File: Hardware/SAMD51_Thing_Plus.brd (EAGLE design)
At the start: 22.9 x 58.4 mm, 114 parts, among them J6 AMP FCI 10103594-0001LF, Q1 2.5A/30V, U1 MCP73831, U2 ATSAMD51J20A-A, U3 AP2112K-3.3V, U4 4MB Flash, Y1 32.768kHz

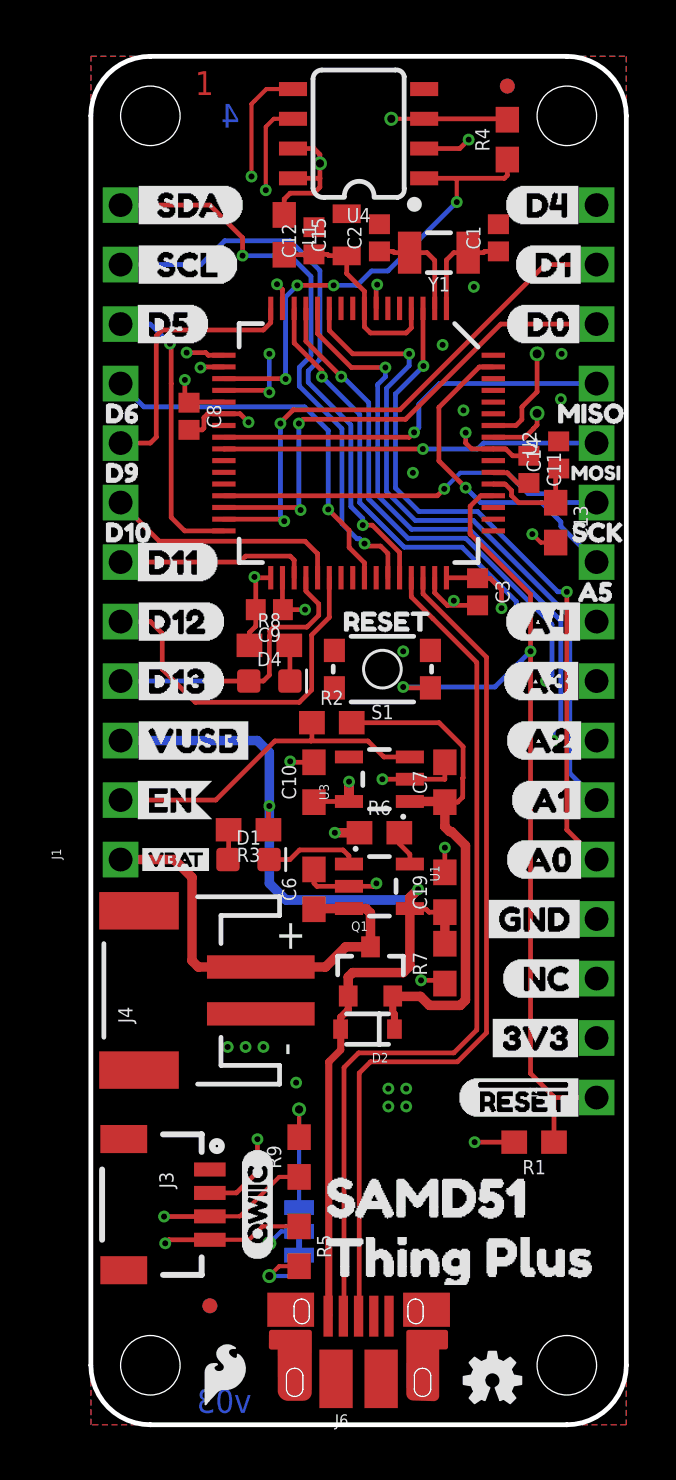
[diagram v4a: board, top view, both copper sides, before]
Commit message: adding i2c labels from double check
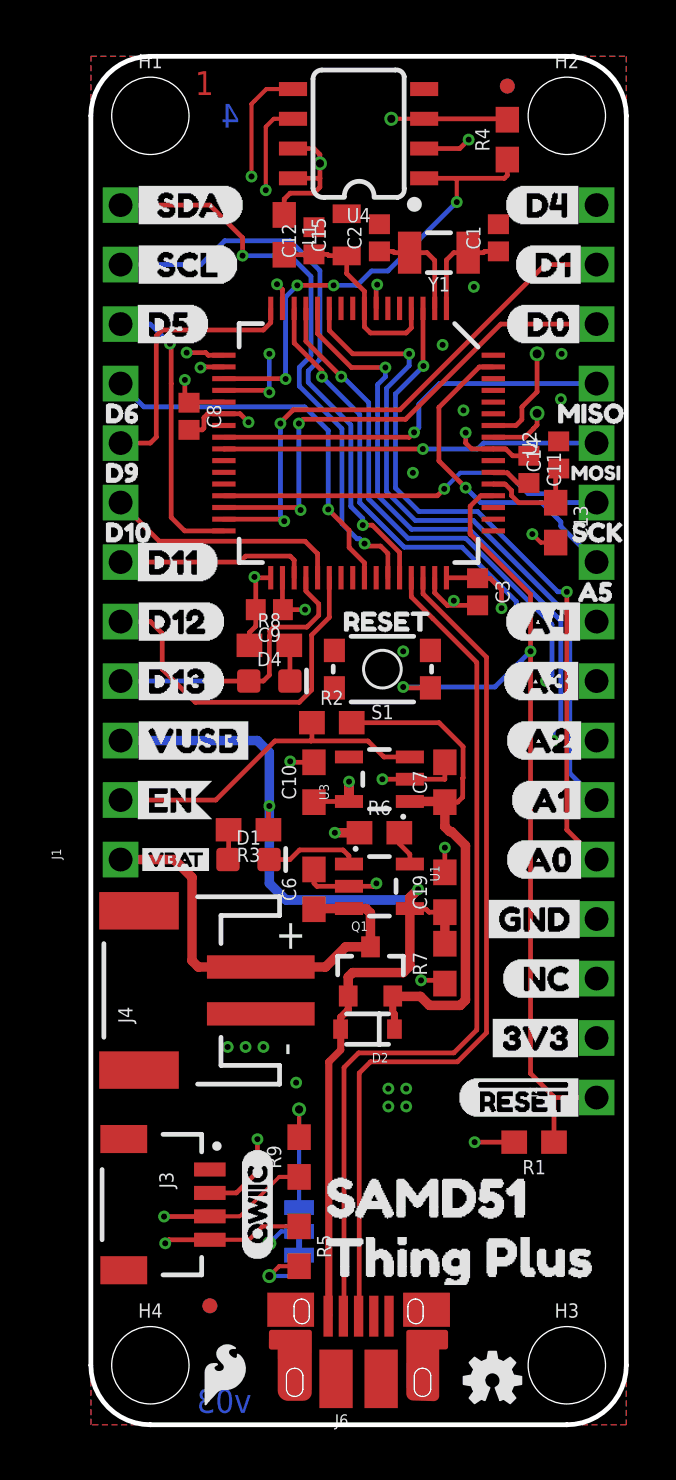
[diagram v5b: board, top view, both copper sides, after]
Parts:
- added H1, H2, H3, H4: STAND-OFF, SparkFun-Hardware:STAND-OFF
- added U$67: (no value), buzzard_labels (39):I_C0
- added U$68: (no value), buzzard_labels (39):21
- turned D1 to 0 degrees
- turned D4 to 0 degrees
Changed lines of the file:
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@@
 <wire x1="0" y1="2.54" x2="0" y2="55.88" width="0.2032" layer="20"/>
 <wire x1="0" y1="55.88" x2="2.54" y2="58.42" width="0.2032" layer="20" curve="-90"/>
-<hole x="2.54" y="55.88" drill="2.54"/>
-<hole x="20.32" y="55.88" drill="2.54"/>
-<hole x="20.32" y="2.54" drill="2.54"/>
-<hole x="2.54" y="2.54" drill="2.54"/>
 <text x="4.445" y="56.769" size="1.016" layer="1" font="vector" ratio="20">1</text>
 <text x="5.461" y="56.769" size="1.016" layer="2" font="vector" ratio="20">2</text>
@@
 <attribute name="PROD_ID" value="SWCH-13065" x="12.446" y="32.258" size="1.778" layer="27" font="vector" ratio="15" rot="R180" display="off"/>
 </element>
-<element name="FRAME1" library="SparkFun-Aesthetics" package="CREATIVE_COMMONS" value="FRAME-LEDGER" x="-17.145" y="-19.05"/>
+<element name="FRAME1" library="SparkFun-Aesthetics" package="CREATIVE_COMMONS" value="FRAME-LEDGER" x="-17.145" y="-19.05">
+<attribute name="DESIGNER" value="" x="-17.145" y="-19.05" size="1.778" layer="27" display="off"/>
+<attribute name="REV" value="" x="-17.145" y="-19.05" size="1.778" layer="27" display="off"/>
+</element>
 <element name="C7" library="SparkFun-Capacitors" package="0603" value="1.0uF" x="15.113" y="27.432" rot="R90">
 <attribute name="PROD_ID" value="CAP-13930" x="32.893" y="13.462" size="1.778" layer="27" font="vector" ratio="15" rot="R90" display="off"/>
@@
 <attribute name="PROD_ID" value="RES-00824" x="37.973" y="-13.335" size="1.778" layer="27" font="vector" ratio="15" rot="R90" display="off"/>
 </element>
-<element name="D1" library="SparkFun-LED" package="LED-0603" value="Yellow" x="6.731" y="24.13" rot="R270">
-<attribute name="PROD_ID" value="DIO-09003" x="-23.749" y="59.69" size="1.778" layer="27" font="vector" ratio="15" rot="R270" display="off"/>
+<element name="D1" library="SparkFun-LED" package="LED-0603" value="Yellow" x="6.731" y="24.13">
+<attribute name="PROD_ID" value="DIO-09003" x="-28.829" y="-6.35" size="1.778" layer="27" font="vector" ratio="15" display="off"/>
 </element>
 <element name="R3" library="SparkFun-Resistors" package="0603" value="1K" x="6.731" y="25.4" rot="R180">
@@
 <attribute name="PROD_ID" value="CAP-08280" x="51.943" y="-26.797" size="1.778" layer="27" font="vector" ratio="15" rot="R90" display="off"/>
 </element>
-<element name="D4" library="SparkFun-LED" package="LED-0603" value="BLUE" x="7.62" y="31.75" rot="R270">
-<attribute name="PROD_ID" value="DIO-08575" x="7.62" y="31.75" size="1.778" layer="27" font="vector" ratio="15" rot="R270" display="off"/>
+<element name="D4" library="SparkFun-LED" package="LED-0603" value="BLUE" x="7.62" y="31.75">
+<attribute name="PROD_ID" value="DIO-08575" x="7.62" y="31.75" size="1.778" layer="27" font="vector" ratio="15" display="off"/>
 </element>
 <element name="R8" library="SparkFun-Resistors" package="0603" value="330" x="7.62" y="33.274">
@@
 </element>
 <element name="JP1" library="SparkFun-Jumpers" package="SMT-JUMPER_3_2-NC_TRACE_SILK" value="JUMPER-SMT_3_2-NC_TRACE_SILK" x="8.89" y="8.255" rot="MR270"/>
+<element name="H1" library="SparkFun-Hardware" package="STAND-OFF" value="STAND-OFF" x="2.54" y="55.88"/>
+<element name="H2" library="SparkFun-Hardware" package="STAND-OFF" value="STAND-OFF" x="20.32" y="55.88"/>
+<element name="H3" library="SparkFun-Hardware" package="STAND-OFF" value="STAND-OFF" x="20.32" y="2.54"/>
+<element name="H4" library="SparkFun-Hardware" package="STAND-OFF" value="STAND-OFF" x="2.54" y="2.54"/>
+<element name="U$67" library="buzzard_labels (39)" package="I_C0" value="" x="6.858" y="9.906" rot="MR270"/>
+<element name="U$68" library="buzzard_labels (39)" package="21" value="" x="6.096" y="9.017" rot="MR270"/>
 </elements>
 <signals>
@@
 <wire x1="5.08" y1="52.07" x2="1.27" y2="52.07" width="0.2032" layer="1"/>
 <contactref element="R9" pad="1"/>
-<wire x1="5.08" y1="8.898" x2="6.358" y2="8.898" width="0.1778" layer="1"/>
-<wire x1="8.04" y1="10.58" x2="8.89" y2="10.58" width="0.1778" layer="1"/>
-<wire x1="6.358" y1="8.898" x2="8.04" y2="10.58" width="0.1778" layer="1"/>
+<wire x1="6.342" y1="8.898" x2="5.08" y2="8.898" width="0.1778" layer="1"/>
+<wire x1="8.89" y1="10.58" x2="8.04" y2="10.58" width="0.1778" layer="1"/>
+<wire x1="8.04" y1="10.58" x2="6.358" y2="8.898" width="0.1524" layer="1"/>
+<wire x1="6.358" y1="8.898" x2="6.342" y2="8.898" width="0.1524" layer="1"/>
 </signal>
 <signal name="A0">
@@
 <mfgpreviewcolor name="substratecolor" color="0xFF786E46"/>
 </mfgpreviewcolors>
-<errors>
-</errors>
 </board>
 </drawing>

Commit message: pre-design review changes
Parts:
- J3: device SparkFun-Connectors:1X04_1MM_RA -> SparkFun-Connectors:JST04_1MM_RA
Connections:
- net D1: now also U2.29; no longer U2.31
- net FLASH_MOSI: now also U2.17; no longer U2.18
- net FLASH_SCK: now also U2.18; no longer U2.17
- net SCK: now also U2.26; no longer U2.29
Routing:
- net D1: track 23.2 -> 21.6 mm
- net FLASH_MOSI: track 15.2 -> 14.5 mm
- net FLASH_SCK: track 14.9 -> 15.4 mm
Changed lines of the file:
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@@
 <element name="FD1" library="SparkFun-Aesthetics" package="MICRO-FIDUCIAL" value="FIDUCIALUFIDUCIAL" x="5.08" y="5.08"/>
 <element name="FD2" library="SparkFun-Aesthetics" package="MICRO-FIDUCIAL" value="FIDUCIALUFIDUCIAL" x="17.78" y="57.15"/>
-<element name="J3" library="SparkFun-Connectors" package="1X04_1MM_RA" value="" x="5.08" y="9.398" rot="R270">
+<element name="J3" library="SparkFun-Connectors" package="JST04_1MM_RA" value="" x="5.08" y="9.398" rot="R270">
 <attribute name="PROD_ID" value="CONN-13694" x="5.08" y="9.398" size="1.778" layer="27" font="vector" ratio="15" rot="R270" display="off"/>
 </element>
@@
 <via x="18.8468" y="38.0238" extent="1-16" drill="0.254"/>
 <via x="16.35125" y="48.5775" extent="1-16" drill="0.254"/>
-<via x="13.74775" y="40.64" extent="1-16" drill="0.254"/>
+<via x="13.74775" y="40.259" extent="1-16" drill="0.254"/>
 <wire x1="19.84375" y1="37.66275" x2="19.20785" y2="37.66275" width="0.1778" layer="1"/>
 <wire x1="19.20785" y1="37.66275" x2="18.8468" y2="38.0238" width="0.1778" layer="1"/>
@@
 <signal name="FLASH_SCK">
 <contactref element="U4" pad="6"/>
-<contactref element="U2" pad="17"/>
 <wire x1="7.487" y1="52.705" x2="7.4676" y2="52.705" width="0.2032" layer="1"/>
 <via x="7.4676" y="52.705" extent="1-16" drill="0.254"/>
-<via x="4.0894" y="45.7708" extent="1-16" drill="0.254"/>
+<via x="4.0894" y="45.2628" extent="1-16" drill="0.254"/>
 <wire x1="5.969" y1="52.705" x2="4.1148" y2="50.8508" width="0.2032" layer="2"/>
 <wire x1="5.969" y1="52.705" x2="7.4676" y2="52.705" width="0.2032" layer="2"/>
-<wire x1="4.0894" y1="45.7708" x2="4.1148" y2="45.7454" width="0.2032" layer="2"/>
-<wire x1="4.1148" y1="50.8508" x2="4.1148" y2="45.7454" width="0.2032" layer="2"/>
+<wire x1="4.0894" y1="45.2628" x2="4.1148" y2="45.2374" width="0.2032" layer="2"/>
+<wire x1="4.1148" y1="50.8508" x2="4.1148" y2="45.2374" width="0.2032" layer="2"/>
 <wire x1="7.4676" y1="52.705" x2="7.4676" y2="55.4101" width="0.1778" layer="1"/>
 <wire x1="7.8105" y1="55.753" x2="8.63" y2="55.753" width="0.1778" layer="1"/>
 <wire x1="7.4676" y1="55.4101" x2="7.8105" y2="55.753" width="0.1778" layer="1"/>
-<wire x1="5.68" y1="45.66" x2="5.013" y2="45.66" width="0.2032" layer="1"/>
-<wire x1="4.9022" y1="45.7708" x2="4.0894" y2="45.7708" width="0.2032" layer="1"/>
-<wire x1="5.013" y1="45.66" x2="4.9022" y2="45.7708" width="0.2032" layer="1"/>
+<contactref element="U2" pad="18"/>
+<wire x1="5.68" y1="45.16" x2="4.1922" y2="45.16" width="0.2032" layer="1"/>
+<wire x1="4.1922" y1="45.16" x2="4.0894" y2="45.2628" width="0.2032" layer="1"/>
 </signal>
 <signal name="V_USB">
@@
 <signal name="FLASH_MOSI">
 <contactref element="U4" pad="5"/>
-<contactref element="U2" pad="18"/>
 <via x="6.858" y="53.2892" extent="1-16" drill="0.254"/>
-<wire x1="4.8875" y1="45.16" x2="5.68" y2="45.16" width="0.2032" layer="1"/>
-<via x="4.67955" y="45.12985" extent="1-16" drill="0.254"/>
+<via x="4.67955" y="45.89185" extent="1-16" drill="0.254"/>
 <wire x1="6.858" y1="53.2892" x2="4.699" y2="51.1302" width="0.2032" layer="15"/>
-<wire x1="4.699" y1="45.1493" x2="4.67955" y2="45.12985" width="0.2032" layer="15"/>
-<wire x1="4.699" y1="51.1302" x2="4.699" y2="45.1493" width="0.2032" layer="15"/>
-<wire x1="4.67955" y1="45.12985" x2="4.85735" y2="45.12985" width="0.2032" layer="1"/>
-<wire x1="4.85735" y1="45.12985" x2="4.8875" y2="45.16" width="0.2032" layer="1"/>
+<wire x1="4.699" y1="45.9113" x2="4.67955" y2="45.89185" width="0.2032" layer="15"/>
+<wire x1="4.699" y1="51.1302" x2="4.699" y2="45.9113" width="0.2032" layer="15"/>
 <wire x1="8.63" y1="57.023" x2="7.493" y2="57.023" width="0.1778" layer="1"/>
-<wire x1="7.493" y1="57.023" x2="6.985" y2="56.515" width="0.1778" layer="1"/>
-<wire x1="6.858" y1="56.388" x2="6.985" y2="56.515" width="0.1778" layer="1"/>
+<wire x1="7.493" y1="57.023" x2="6.858" y2="56.388" width="0.1778" layer="1"/>
 <wire x1="6.858" y1="53.2892" x2="6.858" y2="56.388" width="0.1778" layer="1"/>
+<contactref element="U2" pad="17"/>
+<wire x1="4.67955" y1="45.89185" x2="4.9114" y2="45.66" width="0.2032" layer="1"/>
+<wire x1="4.9114" y1="45.66" x2="5.68" y2="45.66" width="0.2032" layer="1"/>
 </signal>
 <signal name="N$17">
@@
 <signal name="SCK">
 <contactref element="J2" pad="11"/>
-<contactref element="U2" pad="29"/>
 <wire x1="21.59" y1="39.37" x2="20.22381875" y2="39.37" width="0.2032" layer="16"/>
 <wire x1="20.22381875" y1="39.37" x2="19.84281875" y2="39.751" width="0.2032" layer="16"/>
 <wire x1="18.669" y1="39.751" x2="17.78" y2="40.64" width="0.2032" layer="16"/>
 <wire x1="19.84281875" y1="39.751" x2="18.669" y2="39.751" width="0.2032" layer="16"/>
-<via x="15.0876" y="39.9542" extent="1-16" drill="0.254"/>
-<wire x1="15.0876" y1="39.9542" x2="14.7934" y2="39.66" width="0.2032" layer="1"/>
-<wire x1="14.7934" y1="39.66" x2="5.68" y2="39.66" width="0.2032" layer="1"/>
-<wire x1="17.78" y1="40.64" x2="15.7734" y2="40.64" width="0.1778" layer="16"/>
-<wire x1="15.7734" y1="40.64" x2="15.0876" y2="39.9542" width="0.1778" layer="16"/>
+<via x="14.3256" y="40.8432" extent="1-16" drill="0.254"/>
+<wire x1="17.78" y1="40.64" x2="14.5288" y2="40.64" width="0.1778" layer="16"/>
+<wire x1="14.5288" y1="40.64" x2="14.3256" y2="40.8432" width="0.1778" layer="16"/>
+<contactref element="U2" pad="26"/>
+<wire x1="14.3256" y1="40.8432" x2="14.0088" y2="41.16" width="0.2032" layer="1"/>
+<wire x1="14.0088" y1="41.16" x2="5.68" y2="41.16" width="0.2032" layer="1"/>
 </signal>
 <signal name="MOSI">
@@
 <signal name="D1">
 <contactref element="J2" pad="15"/>
-<contactref element="U2" pad="31"/>
 <wire x1="19.3929" y1="49.53" x2="13.1913" y2="43.3284" width="0.2032" layer="1"/>
 <via x="8.0930125" y="42.7442" extent="1-16" drill="0.254"/>
 <wire x1="8.638425" y1="43.3284" x2="8.0930125" y2="42.7829875" width="0.2032" layer="1"/>
 <wire x1="13.1913" y1="43.3284" x2="8.638425" y2="43.3284" width="0.2032" layer="1"/>
-<wire x1="8.0930125" y1="42.7442" x2="8.0930125" y2="38.7377875" width="0.2032" layer="16"/>
-<via x="8.255" y="38.5758" extent="1-16" drill="0.254"/>
-<wire x1="5.68" y1="38.66" x2="8.1708" y2="38.66" width="0.2032" layer="1"/>
-<wire x1="8.1708" y1="38.66" x2="8.255" y2="38.5758" width="0.2032" layer="1"/>
-<wire x1="8.0930125" y1="38.7377875" x2="8.255" y2="38.5758" width="0.2032" layer="16"/>
+<wire x1="8.0930125" y1="42.7442" x2="8.0930125" y2="40.0077875" width="0.2032" layer="16"/>
 <wire x1="8.0930125" y1="42.7829875" x2="8.0930125" y2="42.7442" width="0.2032" layer="1"/>
 <wire x1="21.59" y1="49.53" x2="19.3929" y2="49.53" width="0.2032" layer="1"/>
+<contactref element="U2" pad="29"/>
+<wire x1="8.0930125" y1="40.0077875" x2="7.836225" y2="39.751" width="0.2032" layer="16"/>
+<wire x1="7.836225" y1="39.751" x2="7.62" y2="39.751" width="0.2032" layer="16"/>
+<via x="7.62" y="39.751" extent="1-16" drill="0.254"/>
+<wire x1="7.62" y1="39.751" x2="7.529" y2="39.66" width="0.2032" layer="1"/>
+<wire x1="7.529" y1="39.66" x2="5.68" y2="39.66" width="0.2032" layer="1"/>
 </signal>
 <signal name="D7">

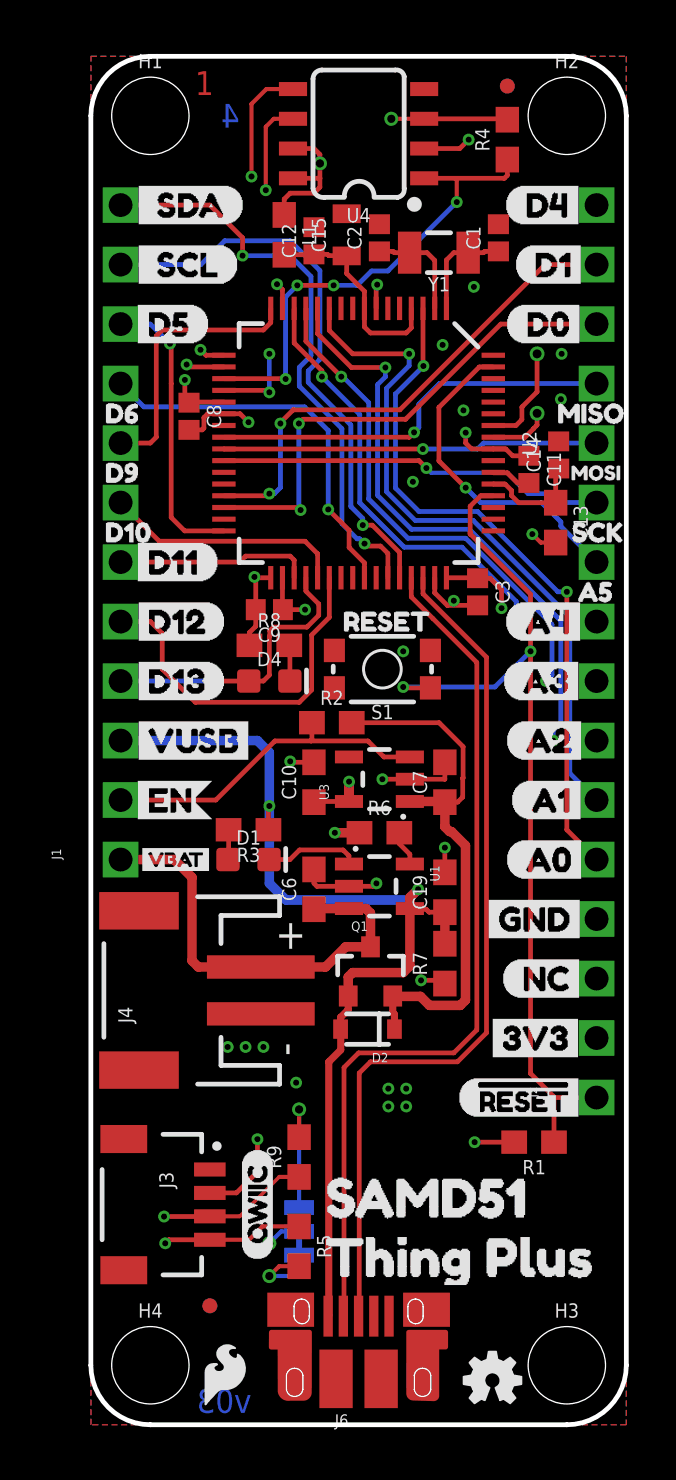
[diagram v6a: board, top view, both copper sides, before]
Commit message: engineer run of checklist-REDS
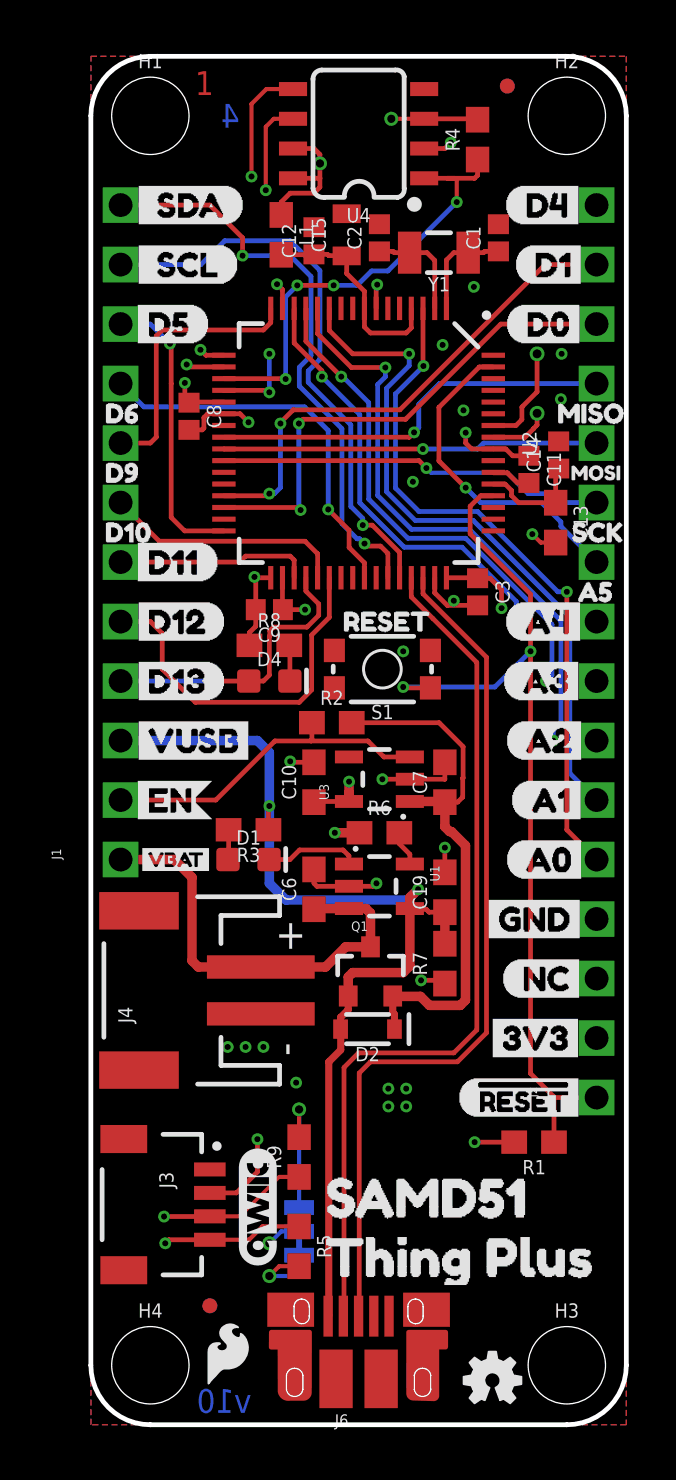
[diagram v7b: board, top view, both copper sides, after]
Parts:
- removed U$45: (no value), buzzard_labels (46):D14
- added U$69: QWIIC_LOGO_5MM, SparkFun-Aesthetics:QWIIC_5MM
- D2: value BAT20J -> 1A/23V/620mV
- FD1, FD2, FD3, FD4: device SparkFun-Aesthetics:MICRO-FIDUCIAL -> SparkFun-Aesthetics:FIDUCIAL-MICRO
- Q1: device SparkFun-DiscreteSemi:SOT23-3 -> SparkFun-DiscreteSemi:SOT23-3@1
- U$41: device buzzard_labels (46):SCK8 -> buzzard_labels (10):21#SCL1
- U$42: device buzzard_labels (46):MOSI7 -> buzzard_labels (10):22#MISO4
- U$43: device buzzard_labels (46):MISO6 -> buzzard_labels (10):23#MOSI3
- U$44: device buzzard_labels (46):D05 -> buzzard_labels (11):1#TX1
- U$47: device buzzard_labels (46):SDA16 -> buzzard_labels (10):24#SCK2
- U$48: device buzzard_labels (46):SCL17 -> buzzard_labels (11):0#RX0
- U$62: device buzzard_labels (46):QWIIC26 -> buzzard_labels (9):20#SDA0
- moved U$62 45.1 mm to (8.64, 52.1), flipped to the bottom, turned to 0 degrees
- moved U$47 19.7 mm to (21.3, 39.4)
- moved U$41 16.6 mm to (8.13, 49.5)
- moved U$48 15.6 mm to (21.3, 47.0)
- moved LOGO3 5.91 mm to (11.4, 53.7)
- moved LOGO4 2.84 mm to (5.84, 3.05)
- moved U$42 2.54 mm to (21.3, 44.5)
- moved U$43 2.54 mm to (21.3, 41.9)
- moved U$44 2.54 mm to (21.3, 49.5)
- moved R4 1.27 mm to (16.5, 54.9)
- moved L1 0.13 mm to (8.13, 50.8)
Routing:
- net 3.3V: track 32.9 -> 30.7 mm
- net FLASH_MISO: track 21.7 -> 20.5 mm
- net FLASH_CS: track 20.4 -> 19.5 mm
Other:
- board text added: "v10"
- board text removed: "v03"
